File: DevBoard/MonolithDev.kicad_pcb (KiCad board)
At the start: 4 copper layers, 196 x 115 mm, 334 parts, among them J101 Pack (welded 4S) - use instea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, J102 Cell NTC 10k 103AT, J103 EV2400 SMBus, J104 Bench PACK_P, J201 SMA OUT_LO, J202 SMA OUT_HI, J301 SWD, J302 UART debug, J303 Spare GPIO, J401 TYPE-C 16PCB0.8 IP68, J402 I2CC logic analyzer, J501 TYPE-C 16PCB0.8 IP68, J502 I2CC logic analyzer, Q101 AGM404AP1, Q102 AGM404AP1, Q103 2N7002, Q401 IAUC45N04S6L063H, Q402 IAUC45N04S6L063H, Q501 IAUC45N04S6L063H, Q502 IAUC45N04S6L063H, SW101 WAKE, SW301 RESET, U101 BQ40Z50RSMR-R2, U201 INA190A5IDDFR, U202 INA190A1IDDFR, U203 TPS70950DBVR, U204 TPS62177DQCR, U301 STM32WB1MMC, U401 TPS25751DREFR, U402 M24512-DFMC6TG, U403 BQ25756RRVR, U404 TPS62933DRLR, U501 TPS25751DREFR, U502 M24512-DFMC6TG, U503 BQ25756RRVR, U504 TPS62933DRLR

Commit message: Dev board: F101 15 A (1206FA-15A) for 100 W output
The 8 A fuse allowed about 6 A continuous after derating, 60-70 W out,
short of the 100 W goal (~10 A from the pack at the 12 V low end).
prosemi 1206FA-15A (C2838894): same 1206 footprint and 300 A at 24 Vdc
interrupt rating. Review doc: gauge OLD ~16-20 A, OCD1 ~10-11 A (2-3 A
in holder mode), output power sharing at 100 W total.

Co-Authored-By: Claude Opus 5.5 <noreply@anthropic.com>
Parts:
- F101: value 8A 32V -> 15A 32V
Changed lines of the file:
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@@
 			)
 		)
-		(property "Value" "8A 32V"
+		(property "Value" "15A 32V"
 			(at 0 1.83 90)
 			(layer "F.Fab")
@@
 			)
 		)
-		(property "Notes" "Hand-fit after checking all four cells at TP102-TP105 (JLC leaves it off). prosemi 1206FA-8A, LCSC C21261118"
+		(property "Notes" "Hand-fit after checking all four cells at TP102-TP105 (JLC leaves it off). 15 A for 100 W out at the 12 V low end (~10 A continuous, 75 % derating). Interrupt 300 A at 24 Vdc (pack max 16.8 V). 3.9 mOhm: 0.4 W at 10 A, give it copper"
 			(at 0 0 90)
 			(layer "F.Fab")
@@
 			)
 		)
-		(property "LCSC" "C21261118"
+		(property "LCSC" "C2838894"
 			(at 0 0 90)
 			(layer "F.Fab")
@@
 			)
 		)
-		(property "MPN" "prosemi 1206FA-8A"
+		(property "MPN" "prosemi 1206FA-15A"
 			(at 0 0 90)
 			(layer "F.Fab")

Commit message: Dev board: bootstrap diodes, one NTC per cell, 1 % resistors
- BQ25756 bootstrap Schottkys DRV_SUP -> BTST1/BTST2 on both ports
  (TI BQ25756 schematic checklist D2/D3, required; LRB521S-40T1G,
  SOD-523), placed in line with the BTST caps. Also added to the
  production BOM/netlist.
- Gauge TS2-TS4 no longer tied to VSS: J105-J107 take a wired 10k NTC
  per cell; all four NTC headers sit beside their cell's tap test point.
- Precision resistors rounded to stocked UNI-ROYAL 1 % parts (ICHG
  9.1k, ILIM 3.6k, TS 1.8k/5.6k, FSW/ACUV-ACOV, NTC dividers); only the
  charge-voltage and PP5V feedback dividers stay 0.1 %.

Co-Authored-By: Claude Opus 5.5 <noreply@anthropic.com>
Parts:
- added D404: LRB521S-40, Diode_SMD:D_SOD-523, F.Cu at (214.2, 76.2)
- added D405: LRB521S-40, Diode_SMD:D_SOD-523, F.Cu at (201.8, 76.2)
- added D504: LRB521S-40, Diode_SMD:D_SOD-523, F.Cu at (214.2, 113.2)
- added D505: LRB521S-40, Diode_SMD:D_SOD-523, F.Cu at (201.8, 113.2)
- added J105: Cell 2 NTC 10k 103AT, Connector_PinHeader_2.54mm:PinHeader_1x02_P2.54mm_Vertical, F.Cu at (156.3, 97.0)
- added J106: Cell 3 NTC 10k 103AT, Connector_PinHeader_2.54mm:PinHeader_1x02_P2.54mm_Vertical, F.Cu at (156.3, 125.0)
- added J107: Cell 4 NTC 10k 103AT, Connector_PinHeader_2.54mm:PinHeader_1x02_P2.54mm_Vertical, F.Cu at (156.3, 153.0)
- J102: value Cell NTC 10k 103AT -> Cell 1 NTC 10k 103AT
- R308, R309, R310, R311, R411, R511: value 10.0k 0.1% -> 10k 1%
- R409, R509: value 137k 0.1% -> 137k 1%; footprint Resistor_SMD:R_0805_2012Metric -> Resistor_SMD:R_0603_1608Metric
- R410, R412, R510, R512: value 40.2k 0.1% -> 40.2k 1%
- R413, R513: value 9.09k 0.1% -> 9.1k 1%
- R414, R514: value 3.65k 0.1% -> 3.6k 1%
- R415, R515: value 1.74k 0.1% -> 1.8k 1%
- R416, R516: value 5.11k 0.1% -> 5.6k 1%
- moved J102 78.3 mm to (156.3, 70.0)
- moved R409 0.22 mm to (218.6, 70.6)
- moved R509 0.22 mm to (218.6, 107.6)
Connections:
- net Net-(U403-DRV_SUP) renamed /USB Port 1/DRV_SUP
- net Net-(U503-DRV_SUP) renamed /USB Port 2/DRV_SUP
- U101 pad 11: CELL_N -> /Cells and Gauge/TS2
- U101 pad 12: CELL_N -> /Cells and Gauge/TS3
- U101 pad 13: CELL_N -> /Cells and Gauge/TS4

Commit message: Dev board rev A5: FET ESD caps, review 2, fail-safe CHG_INH, MCU I/O plan
- Gauge: C110/C111 (2 x 0.1 uF in series) across the protection FET pair,
  TI BQ40Z50-R2 fig. 9-2 C1/C2; C107/C108 across PACK+/PACK- unchanged.
- Second 3-reviewer schematic review with a challenge round
  (docs/devboard/schematic-review-2-2026-10-12.md, raw files in review2/):
  0 critical, 1 major (gauge precharge config), hardware proposals listed.
- CHG_INH now fails safe: R417/R517 47k pull-up on CE to 3V3; the MCU
  drives PB8 low to allow charging. MCU IWDG in hardware mode.
- Decisions: ICHG stays 9.1k; F101 stays 15 A with a gauge cut-off of
  2.8 V/cell or higher under load.
- docs/devboard/mcu-io-power-states.md: every MCU pin per power state,
  reconciled with the 150 uA sleep budget (PB8 low only while charging).

Co-Authored-By: Claude Opus 5.5 <noreply@anthropic.com>
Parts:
- added C110: 0.1u 50V, Capacitor_SMD:C_0603_1608Metric, F.Cu at (177.8, 78.0)
- added C111: 0.1u 50V, Capacitor_SMD:C_0603_1608Metric, F.Cu at (181.2, 78.0)
- R417, R517: value 10k -> 47k
- moved JP202 0.20 mm to (188.1, 140.1)
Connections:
- R417 pad 2: GND -> 3V3
- R517 pad 2: GND -> 3V3

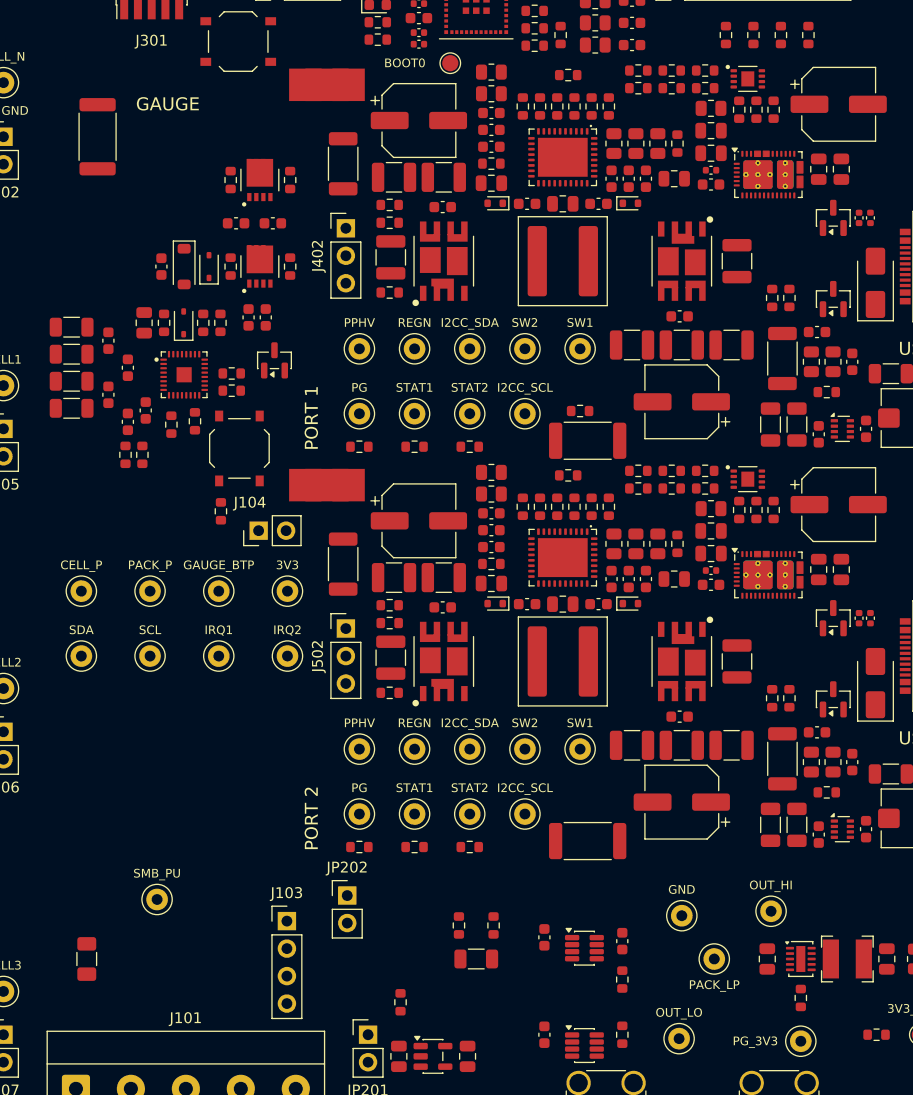
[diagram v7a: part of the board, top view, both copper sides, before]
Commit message: Dev board rev A5: BAT fed before F101, review 2 hardware fixes, JLC passives
- Gauge BAT feed follows TI fig. 9-12: D101 from the cell top (CELL_P_RAW)
  before F101, so the gauge stays powered if the fuse opens or is unfitted.
- C421/C521 100 uF 35 V polymer (same 6.3 mm footprint): about 99 uF worst
  case vs the BQ25756 80 uF minimum after derating.
- Bootstrap diodes LRB520S-40T1G, Q103 BSS138, DNP C109 4.7 nF (fit D103
  with it), PPHV 0.1 uF and VBUS 10 nF per port, R306 330R, C201 DNP flag.
- Test points: GND loops by each port's SW probes and in the pack probe
  field, CELL_P_RAW, CE_N, LDO_3V3, LDO_IN, 5V_AMP.
- JLC part numbers on every resistor and capacitor.
- Placement for the new parts; placer hides test-point labels with no
  free spot. DRC clean, schematic parity clean.

Co-Authored-By: Claude Opus 5.5 <noreply@anthropic.com>
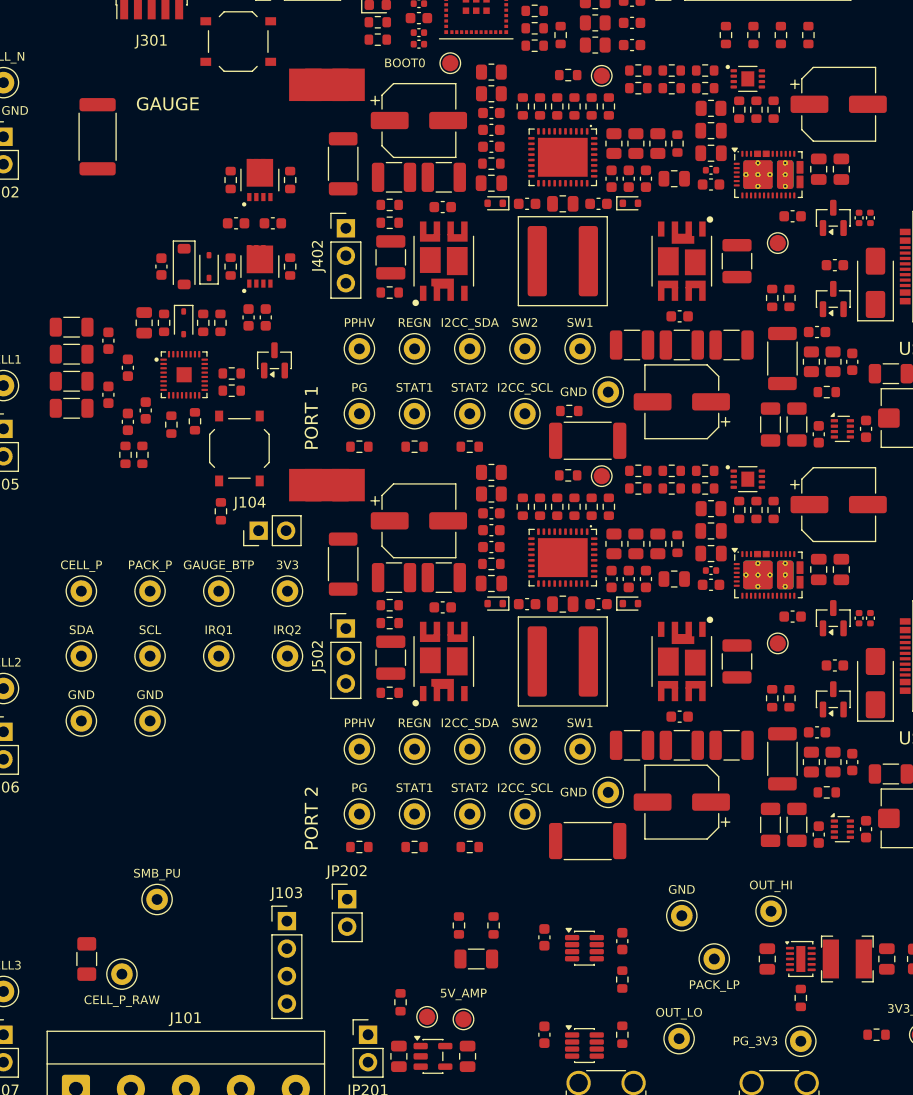
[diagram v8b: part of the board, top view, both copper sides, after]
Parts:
- added C449: 0.1u 50V, Capacitor_SMD:C_0603_1608Metric, F.Cu at (229.2, 77.3)
- added C450: 10n 50V, Capacitor_SMD:C_0603_1608Metric, F.Cu at (233.2, 81.9)
- added C549: 0.1u 50V, Capacitor_SMD:C_0603_1608Metric, F.Cu at (229.2, 114.3)
- added C550: 10n 50V, Capacitor_SMD:C_0603_1608Metric, F.Cu at (233.2, 118.9)
- added TP108: CELL_P_RAW, TestPoint:TestPoint_Keystone_5000-5004_Miniature, F.Cu at (167.2, 147.4)
- added TP109: GND, TestPoint:TestPoint_Keystone_5000-5004_Miniature, F.Cu at (163.5, 124.0)
- added TP206: LDO_IN, TestPoint:TestPoint_Pad_D1.5mm, F.Cu at (195.5, 151.3)
- added TP207: 5V_AMP, TestPoint:TestPoint_Pad_D1.5mm, F.Cu at (198.8, 151.6)
- added TP309: GND, TestPoint:TestPoint_Keystone_5000-5004_Miniature, F.Cu at (169.8, 124.0)
- added TP412: GND, TestPoint:TestPoint_Keystone_5000-5004_Miniature, F.Cu at (212.2, 93.6)
- added TP413: CE_N, TestPoint:TestPoint_Pad_D1.5mm, F.Cu at (211.6, 64.4)
- added TP414: LDO_3V3, TestPoint:TestPoint_Pad_D1.5mm, F.Cu at (227.9, 79.8)
- added TP512: GND, TestPoint:TestPoint_Keystone_5000-5004_Miniature, F.Cu at (212.2, 130.6)
- added TP513: CE_N, TestPoint:TestPoint_Pad_D1.5mm, F.Cu at (211.6, 101.4)
- added TP514: LDO_3V3, TestPoint:TestPoint_Pad_D1.5mm, F.Cu at (227.9, 116.8)
- C101, C102, C103, C104, C412, C413, C440, C512, C513, C540: value 0.1u 25V -> 0.1u 50V
- C109: value 0.1u 50V -> 4.7n 50V
- C201: value 22n DNP -> 22n 50V
- C207: value 22u 10V -> 22u 25V
- C407, C507: value 10u 10V -> 10u 25V
- C410, C411, C510, C511: value 4.7u 16V -> 4.7u 25V
- C421, C521: value 68u 35V -> 100u 35V; footprint Capacitor_SMD:CP_Elec_6.3x5.8 -> Capacitor_SMD:CP_Elec_6.3x7.7
- C439, C539: value 33n -> 33n 50V
- C441, C442, C541, C542: value 22u 35V -> 22u 25V
- D404, D405, D504, D505: value LRB521S-40 -> LRB520S-40T1G
- Q103: value 2N7002 -> BSS138
- R306: value 1k -> 330
- moved TH304 1.00 mm to (208.6, 95.3)
- moved JP202 0.34 mm to (188.1, 140.5)
- turned D101 to -90 degrees
- turned SW101 to -90 degrees
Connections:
- D101 pad 2: /Cells and Gauge/CELL_P -> /Cells and Gauge/CELL_P_RAW
